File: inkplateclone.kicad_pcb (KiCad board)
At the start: 2 copper layers, 78.9 x 50.1 mm, 44 parts, among them J2 Conn_01x16_Male, U1 TPS65186, U2 ED097OC1, U3 MCP23017_SO

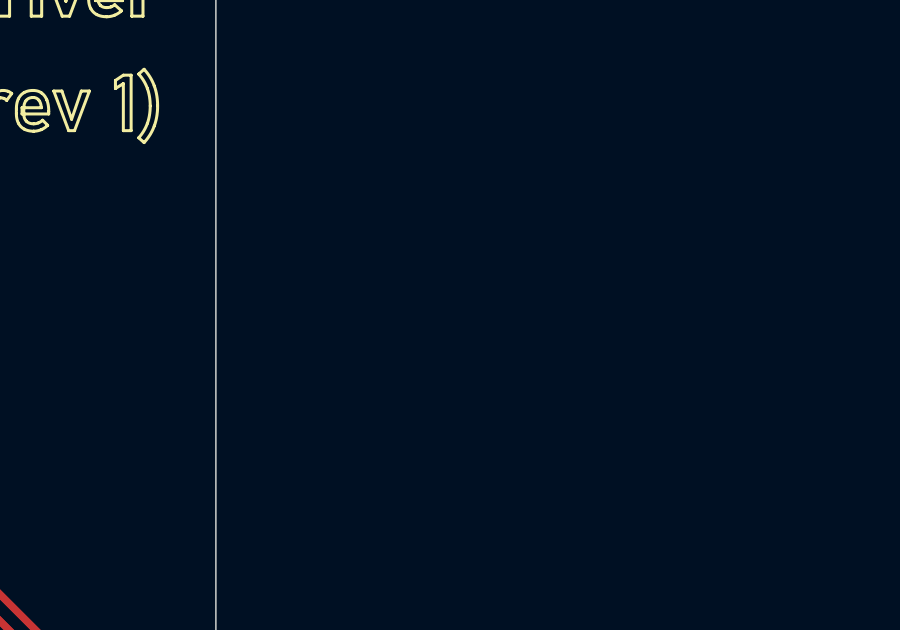
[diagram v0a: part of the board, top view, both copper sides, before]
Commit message: cleanup schematic, early pcb work for the 6 inch connector
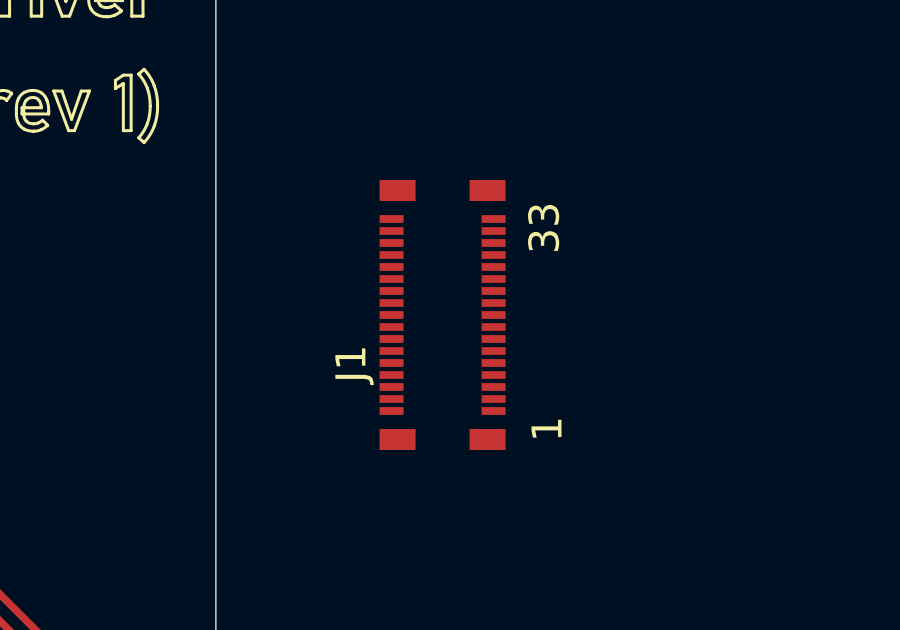
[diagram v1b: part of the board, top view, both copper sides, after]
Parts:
- added J1: ED060SC7, inkplateclone:PANASONIC_AXT334124, F.Cu at (143.5, 80.0)
- C20, C21, C22: value 100n -> 100nF
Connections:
- U3 pad 15: Net-(U3-Pad15) -> GND
- U3 pad 16: Net-(U3-Pad16) -> GND
- U3 pad 17: Net-(U3-Pad17) -> GND

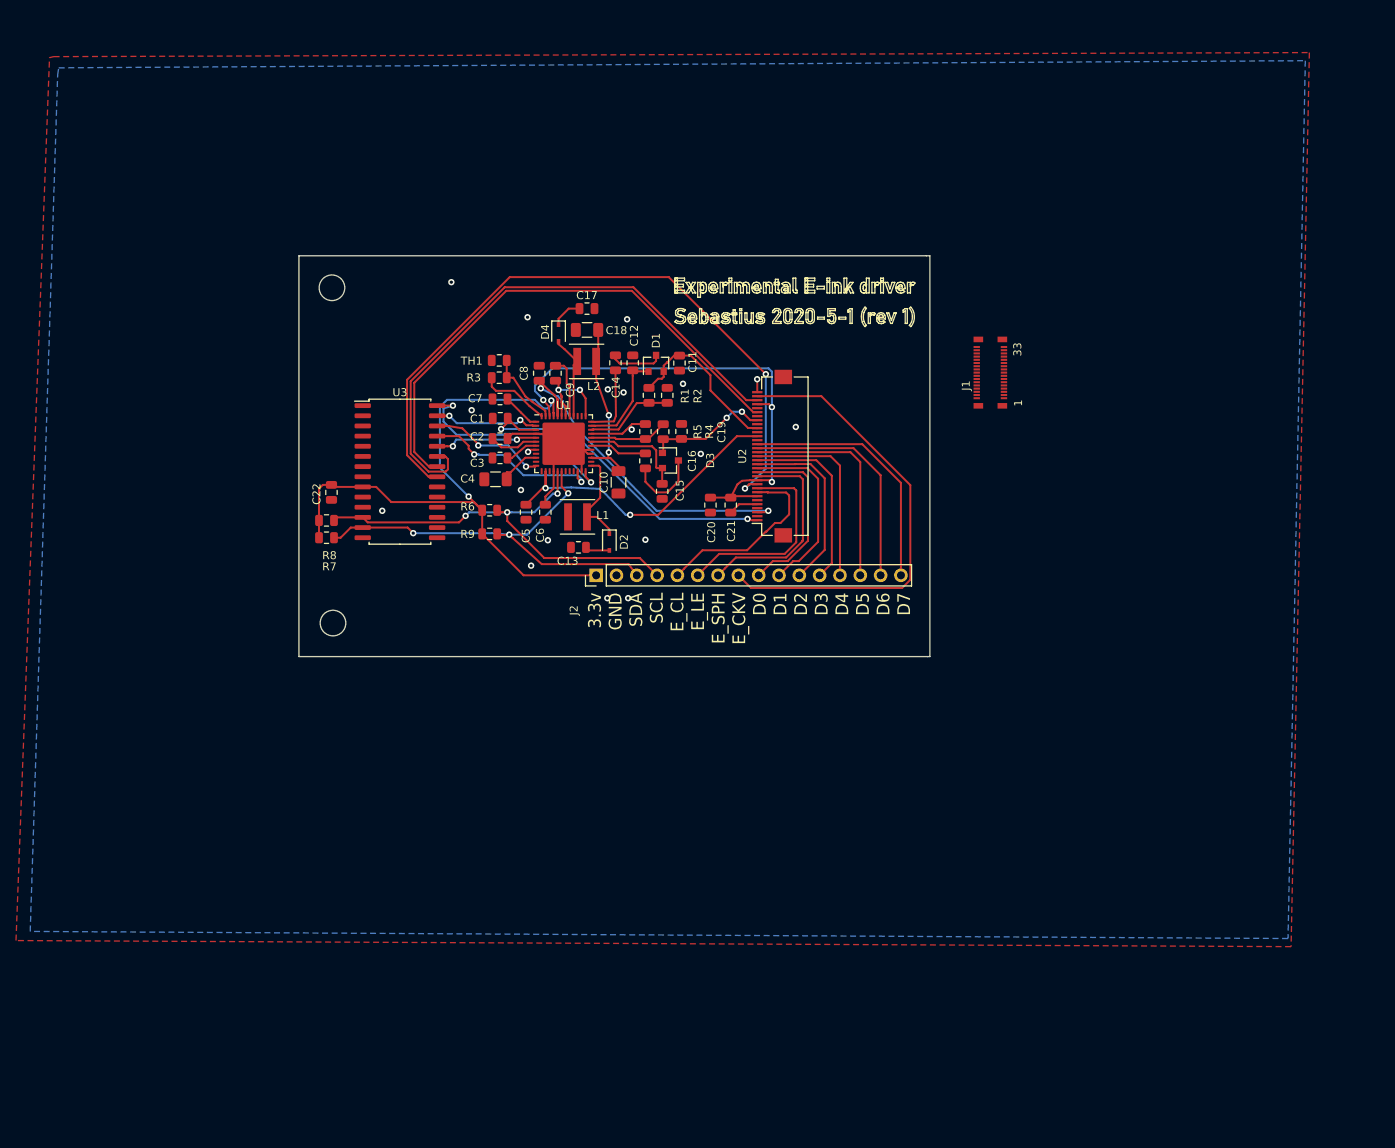
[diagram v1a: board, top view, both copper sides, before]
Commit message: ripped up and made a mess but its cool. Also added cooling pad underneath TPS56186 chip
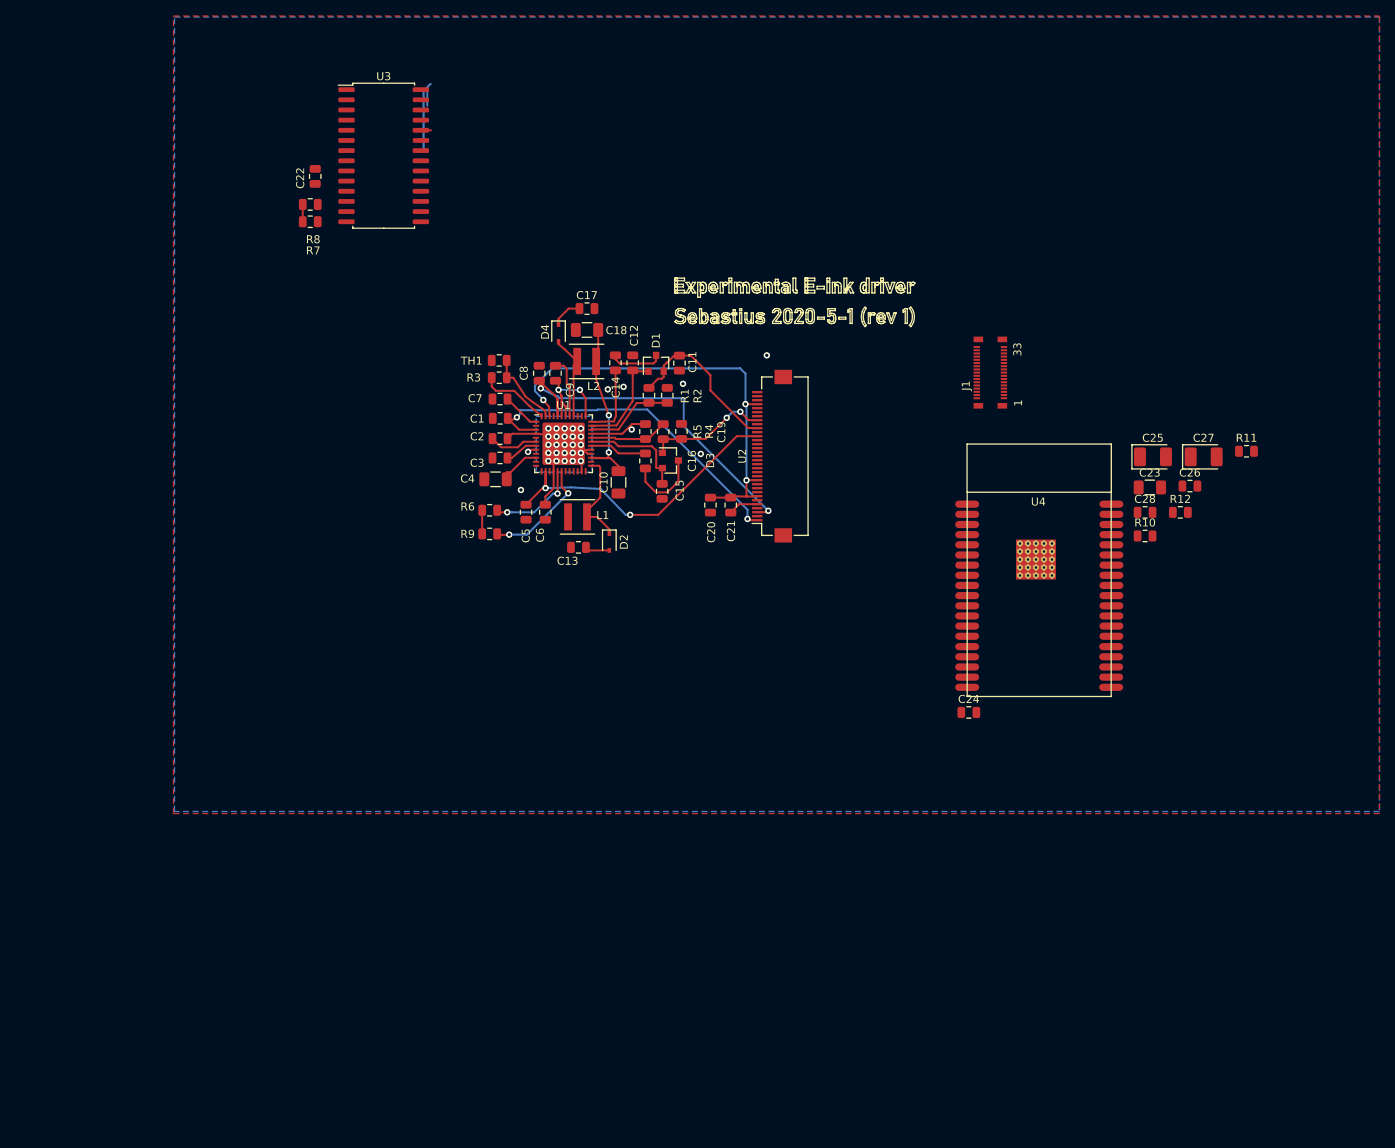
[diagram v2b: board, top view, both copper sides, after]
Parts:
- removed J2: Conn_01x16_Male, Connector_PinHeader_2.54mm:PinHeader_1x16_P2.54mm_Vertical
- removed REF** (x2): MountingHole_3.2mm_M3, MountingHole:MountingHole_3.2mm_M3
- added C23: 10uF, Capacitor_SMD:C_1206_3216Metric, F.Cu at (163.4, 94.4)
- added C24: 2u2, Capacitor_SMD:C_0805_2012Metric, F.Cu at (140.8, 122.5)
- added C25: 68uF, 6.3v, Capacitor_Tantalum_SMD:CP_EIA-3528-15_AVX-H_Pad1.50x2.35mm_HandSolder, F.Cu at (163.8, 90.5)
- added C26: 100nF, Capacitor_SMD:C_0805_2012Metric, F.Cu at (168.5, 94.2)
- added C27: 68uF, 6.3v, Capacitor_Tantalum_SMD:CP_EIA-3528-15_AVX-H_Pad1.50x2.35mm_HandSolder, F.Cu at (170.2, 90.5)
- added C28: 100nF, Capacitor_SMD:C_0805_2012Metric, F.Cu at (162.8, 97.5)
- added R10: 1k, Resistor_SMD:R_0805_2012Metric, F.Cu at (162.8, 100.4)
- added R11: 1k, Resistor_SMD:R_0805_2012Metric, F.Cu at (175.5, 89.8)
- added R12: 1k, Resistor_SMD:R_0805_2012Metric, F.Cu at (167.3, 97.5)
- added U4: ESP32-WROVER, Wrover:ESP32-WROVER, F.Cu at (149.6, 95.5)
- moved R8 39.5 mm to (58.5, 59.0)
- moved U3 39.5 mm to (67.7, 52.9)
- moved C22 39.5 mm to (59.1, 55.5)
- moved R7 39.5 mm to (58.5, 61.2)
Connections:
- net Net-(J1-Pad34) renamed /SPI_SDO
- J1 pad 22: Net-(J1-Pad22) -> /SPI_SCL
- J1 pad 24: Net-(J1-Pad24) -> /SPI_SDI
- J1 pad 33: Net-(J1-Pad33) -> /SPI_NCS
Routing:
- net /EPD_OE: track 86.7 -> 0.00 mm, vias 2 -> 0
- net /EPD_SPV: track 71.6 -> 0.00 mm
- net /EPD_GMODE: track 66.2 -> 0.00 mm
- net +3V3: track 80.0 -> 14.0 mm, vias 2 -> 0
- net /EPD_CKV: track 58.1 -> 0.00 mm
- net /I2C_SCL: track 56.6 -> 11.4 mm, vias 3 -> 2
- net /I2C_SDA: track 55.3 -> 14.5 mm, vias 3 -> 2
- net /EPD_D7: track 31.5 -> 0.00 mm
- net /EPD_D6: track 29.3 -> 0.00 mm
- net /EPD_D5: track 27.5 -> 0.00 mm
- net /PWR_GOOD: track 28.2 -> 1.66 mm, vias 2 -> 0
- net /EPD_SPH: track 25.9 -> 0.00 mm
- net /EPD_LE: track 25.5 -> 0.00 mm
- net /EPD_D4: track 24.5 -> 0.00 mm
- net /EPD_CL: track 23.6 -> 0.00 mm
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- added copper zone on B.Cu, net /VN
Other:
- board outline removed
- board text removed: "3.3v GND SDA SCL E_CL E_LE E_SPH E_CKV D0 D1 D2 D3 D4 D5 D6 D7"

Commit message: added usb C-serial and fixed errors in the tps65186 part of the schematic
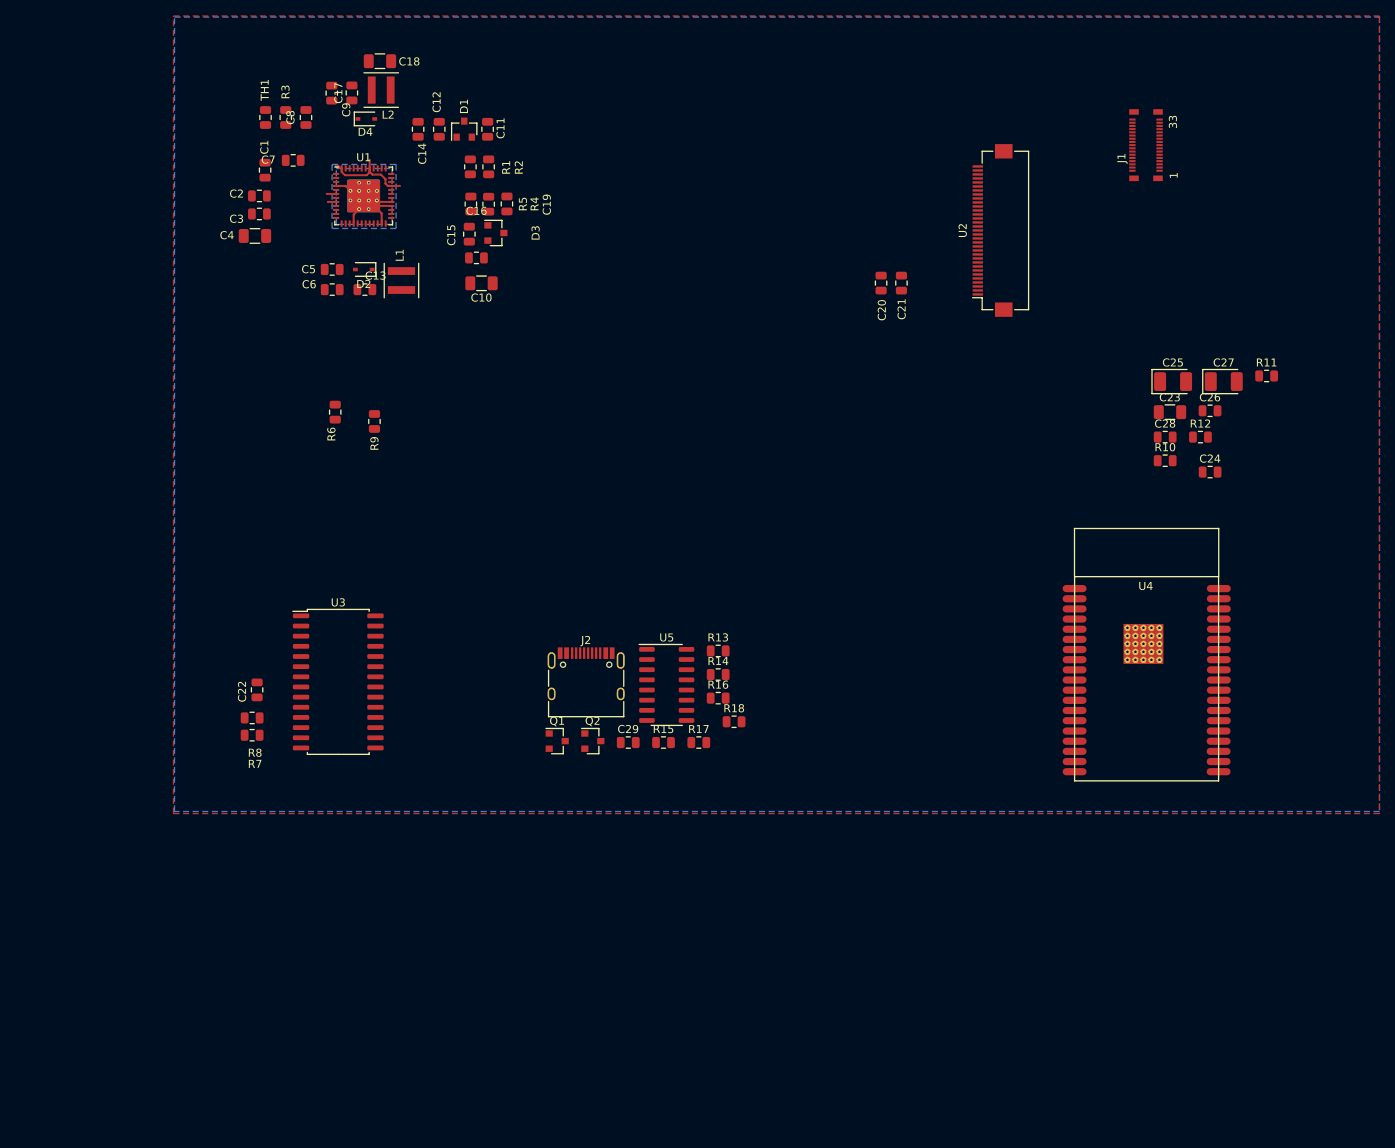
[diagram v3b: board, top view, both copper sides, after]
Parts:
- added C29: 100nF, Capacitor_SMD:C_0805_2012Metric, F.Cu at (98.2, 126.3)
- added J2: USB_C_Receptacle_USB2.0, Connector_USB:USB_C_Receptacle_HRO_TYPE-C-31-M-12, F.Cu at (93.0, 119.1)
- added Q1: Q_NMOS_GSD, Package_TO_SOT_SMD:SOT-23, F.Cu at (89.4, 126.1)
- added Q2: Q_NMOS_GSD, Package_TO_SOT_SMD:SOT-23, F.Cu at (93.8, 126.1)
- added R13: 5.1K, Resistor_SMD:R_0805_2012Metric, F.Cu at (109.5, 114.8)
- added R14: 5.1K, Resistor_SMD:R_0805_2012Metric, F.Cu at (109.5, 117.8)
- added R15: 10K, Resistor_SMD:R_0805_2012Metric, F.Cu at (102.7, 126.3)
- added R16: 10K, Resistor_SMD:R_0805_2012Metric, F.Cu at (109.5, 120.7)
- added R17: 10K, Resistor_SMD:R_0805_2012Metric, F.Cu at (107.1, 126.3)
- added R18: 10K, Resistor_SMD:R_0805_2012Metric, F.Cu at (111.5, 123.7)
- added U5: CH340C, Package_SO:SOIC-16_3.9x9.9mm_P1.27mm, F.Cu at (103.1, 119.1)
- U1: footprint Package_DFN_QFN:QFN-48-1EP_7x7mm_P0.5mm_EP5.3x5.3mm -> TP56186:QFN-48-1EP_7x7mm_P0.5mm_EP5.3x5.3mm_ThermalVias
- moved U3 66.0 mm to (62.0, 118.7)
- moved C22 64.6 mm to (51.9, 119.7)
- moved R7 64.6 mm to (51.2, 125.3)
- moved R8 64.6 mm to (51.2, 123.2)
- moved D2 45.9 mm to (65.2, 67.1), turned to 180 degrees
- moved C9 44.8 mm to (61.2, 45.1)
- moved C8 43.3 mm to (58.0, 48.1)
- moved C3 42.8 mm to (52.1, 60.2)
- moved C4 42.8 mm to (51.6, 62.9)
- moved C1 42.7 mm to (52.9, 54.7), turned to 90 degrees
- moved C2 42.7 mm to (52.1, 57.9)
- moved C24 42.6 mm to (171.0, 92.4)
- moved L2 42.5 mm to (67.4, 44.7)
- moved C18 42.4 mm to (67.2, 41.1)
- moved TH1 42.1 mm to (52.9, 48.1), turned to 270 degrees
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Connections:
- net /EPD_CL renamed EPD_CL
- C13 pad 2: Net-(C13-Pad2) -> /VN
- C17 pad 1: Net-(C17-Pad1) -> /VB
- C4 pad 1: Net-(C4-Pad1) -> /VIN
- D2 pad 2: Net-(C13-Pad2) -> /VN
- D4 pad 1: Net-(C17-Pad1) -> /VB
- U1 pad 10: Net-(C4-Pad1) -> /VIN
- U4 pad 3: /RST -> RST
- U4 pad 34: /RXD -> ESP_RXD
- U4 pad 35: /TXD -> ESP_TXD
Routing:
- net /3V3-EINK: track 56.2 -> 0.00 mm, vias 3 -> 0
- net /VPOS: track 46.6 -> 0.00 mm, vias 2 -> 0
- net /VNEG: track 43.1 -> 0.00 mm, vias 2 -> 0
- net /VCOM: track 39.2 -> 0.00 mm, vias 2 -> 0
- net /VIN: track 23.0 -> 0.00 mm, vias 2 -> 0
- net /VDDH: track 21.3 -> 0.00 mm
- net GND: track 34.9 -> 14.2 mm, vias 8 -> 0
- net /VN: track 28.5 -> 13.0 mm, vias 25 -> 0
- net /VEE: track 15.4 -> 0.00 mm, vias 2 -> 0
- net /I2C_SDA: track 14.5 -> 0.00 mm, vias 2 -> 0
- net +3V3: track 14.0 -> 0.00 mm
- net /VEE_D: track 13.5 -> 0.00 mm
- net /VN_SW: track 13.1 -> 0.00 mm
- net /VDDH_D: track 12.7 -> 0.00 mm
- net /VB: track 12.7 -> 0.00 mm, vias 2 -> 0
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
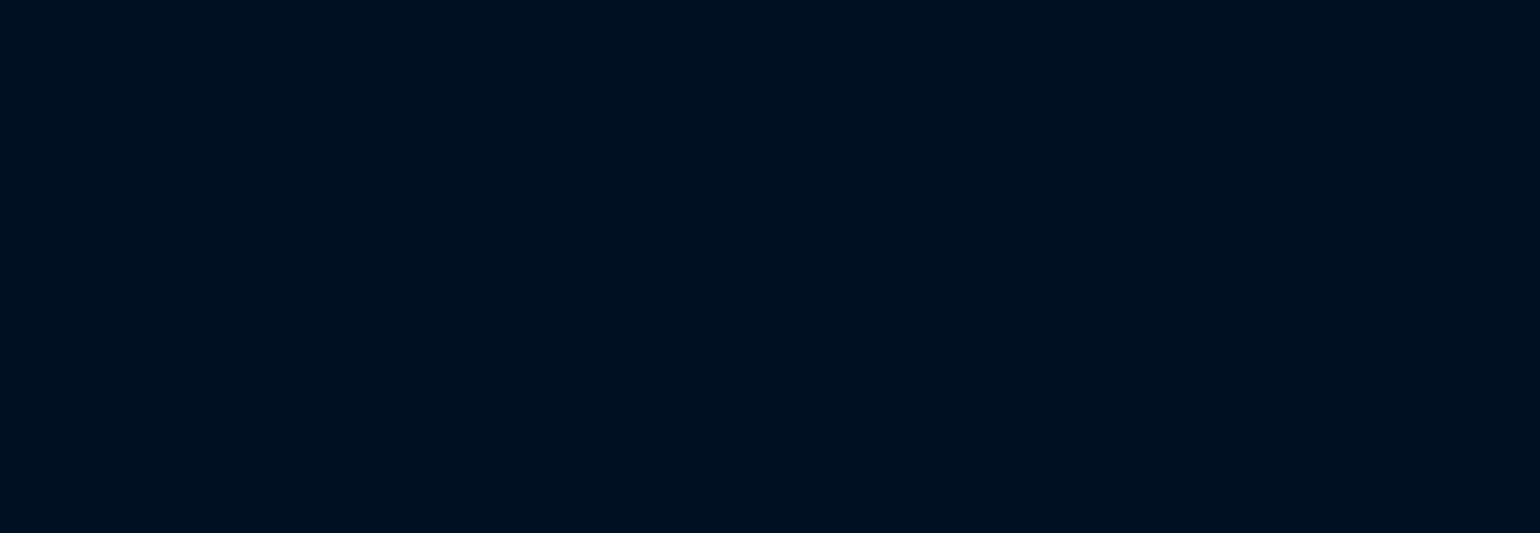
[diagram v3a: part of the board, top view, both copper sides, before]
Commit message: added ideal diode and 3.3v circuit. Battery stuff and inputs still todo
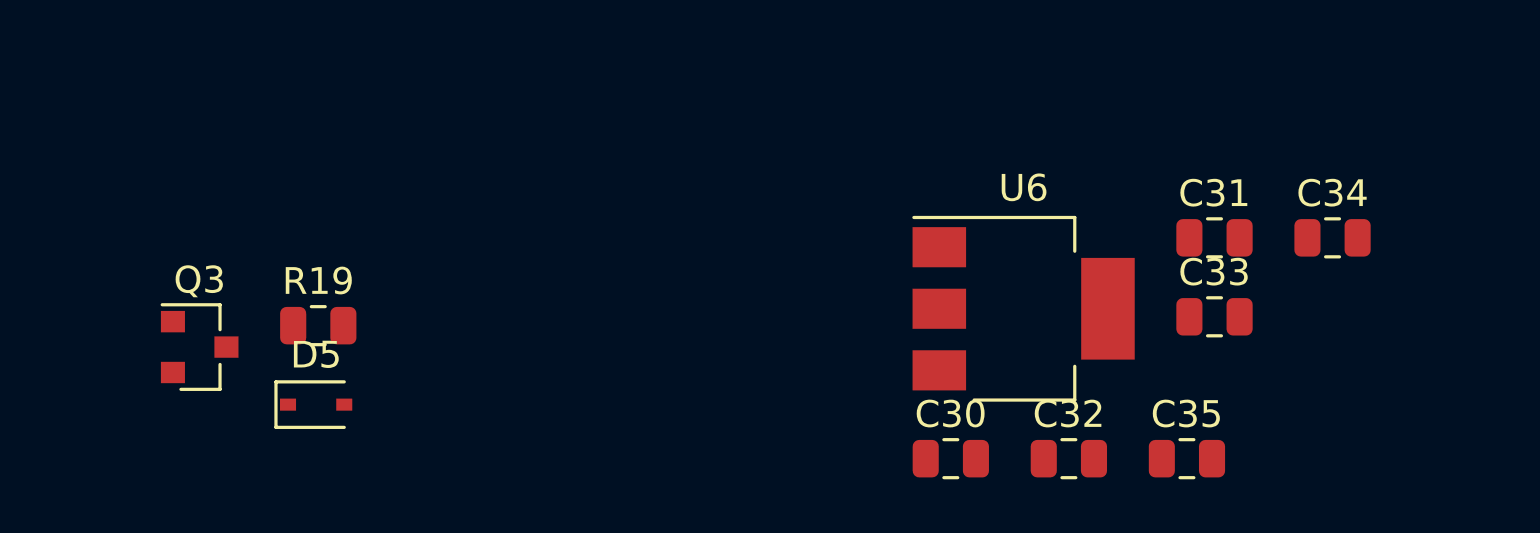
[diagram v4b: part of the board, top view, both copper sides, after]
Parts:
- added C30: 4u7, Capacitor_SMD:C_0805_2012Metric, F.Cu at (136.1, 152.8)
- added C31: 100nF, Capacitor_SMD:C_0805_2012Metric, F.Cu at (145.9, 144.5)
- added C32: 4u7, Capacitor_SMD:C_0805_2012Metric, F.Cu at (140.5, 152.8)
- added C33: 4u7, Capacitor_SMD:C_0805_2012Metric, F.Cu at (145.9, 147.5)
- added C34: 100nF, Capacitor_SMD:C_0805_2012Metric, F.Cu at (150.3, 144.5)
- added C35: 4u7, Capacitor_SMD:C_0805_2012Metric, F.Cu at (144.9, 152.8)
- added D5: BAT20JFILM, Diode_SMD:D_SOD-323, F.Cu at (112.4, 150.8)
- added Q3: Q_PMOS_GSD, Package_TO_SOT_SMD:SOT-23, F.Cu at (108.0, 148.6)
- added R19: 10K, Resistor_SMD:R_0805_2012Metric, F.Cu at (112.4, 147.8)
- added U6: AMS1117-3.3, Package_TO_SOT_SMD:SOT-223-3_TabPin2, F.Cu at (138.8, 147.2)
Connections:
- net /VIN renamed VIN
